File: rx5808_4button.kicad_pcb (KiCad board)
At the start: 2 copper layers, 80 x 65 mm, 60 parts, among them IC1 ATMEGA328-A, P1 CONN_01X02, P10 CONN_01X01, P11 CONN_01X01, P2 CONN_01X05, P3 CONN_02X03, P4 CONN_01X02, P5 BNC, P6 BNC, P7 CONN_01X02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

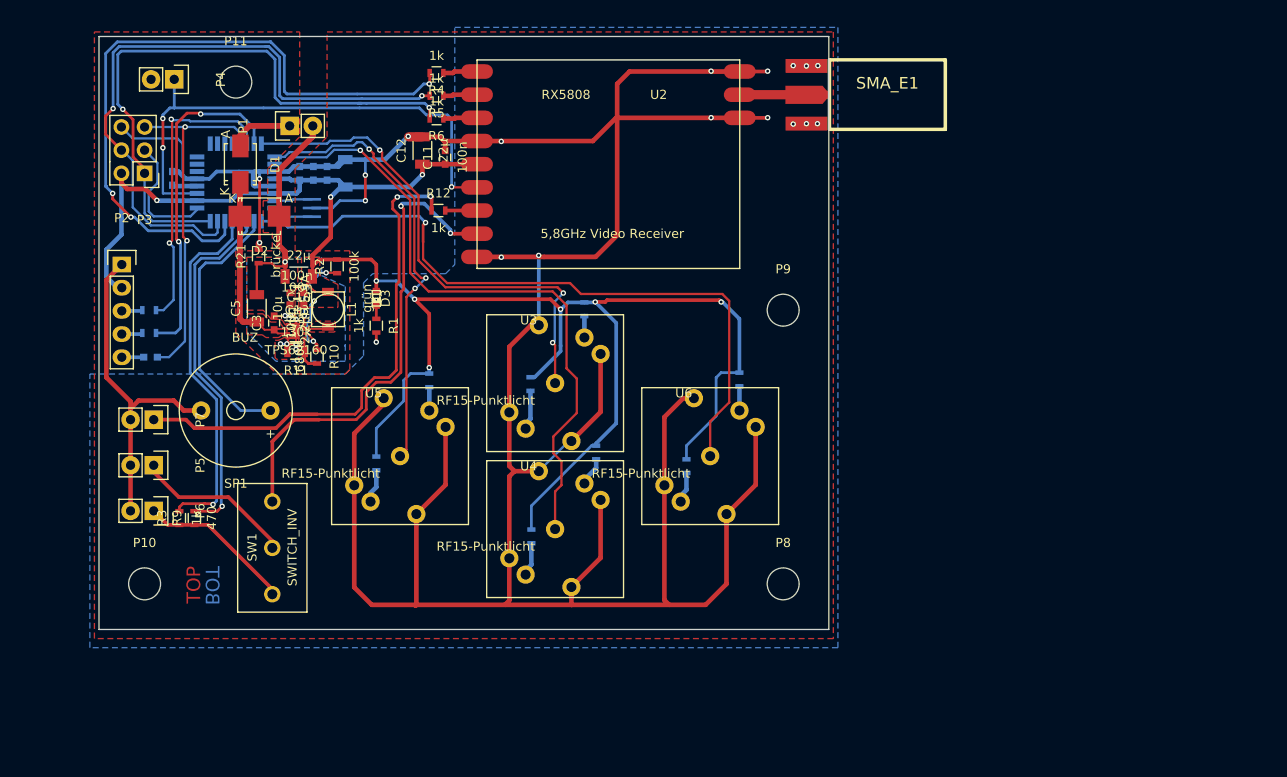
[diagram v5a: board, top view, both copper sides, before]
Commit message: symbol hinzugefügt
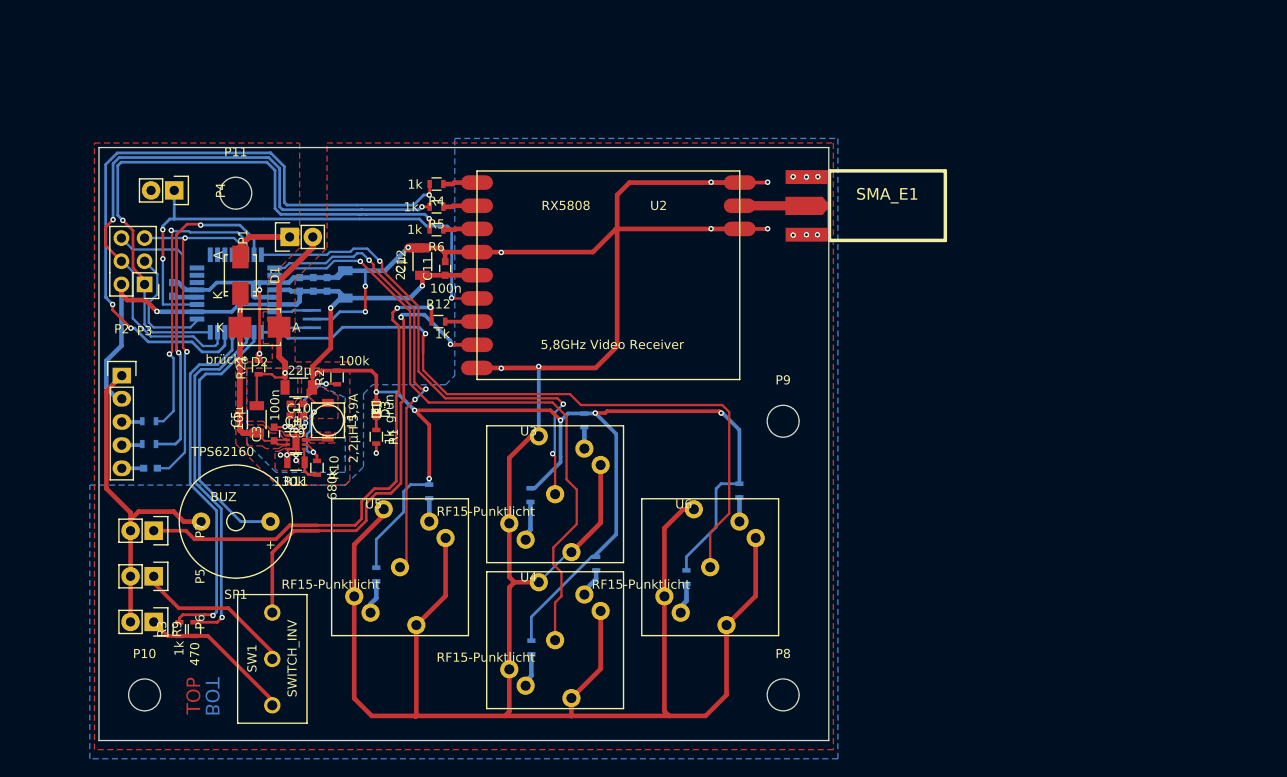
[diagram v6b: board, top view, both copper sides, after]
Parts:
- moved C13 12.2 mm to (105.7, 107.3)
- moved P10 12.2 mm to (89.0, 139.2)
- moved P6 12.2 mm to (90.0, 131.2)
- moved P8 12.2 mm to (159.0, 139.2)
- moved R10 12.2 mm to (107.9, 114.3)
- moved R14 12.2 mm to (131.3, 117.3)
- moved R15 12.2 mm to (138.5, 124.8)
- moved R19 12.2 mm to (154.2, 116.8)
- moved R20 12.2 mm to (148.4, 126.3)
- moved R21 12.2 mm to (101.5, 103.3)
- moved SW1 12.2 mm to (103.0, 135.2)
- moved U4 12.2 mm to (134.0, 133.2)
- moved Y1 12.2 mm to (107.3, 98.0)
- moved C1 12.2 mm to (92.0, 94.7)
- moved C10 12.2 mm to (105.9, 105.5)
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
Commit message: dickbutt inserted
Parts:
- added G***: LOGO, Dickbutt:Kupferdickbutt, F.Cu at (159.4, 98.4)
- P1: footprint Pin_Headers:Pin_Header_Straight_1x02 -> Sockets_MOLEX_KK-System:Socket_MOLEX-KK-RM2-54mm_Lock_2pin_straight
- moved P1 6.71 mm to (107.0, 82.6), turned to 0 degrees
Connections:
- IC1 pad 12: Net-(IC1-Pad12) -> (no net)
- IC1 pad 22: Net-(IC1-Pad22) -> (no net)
- IC1 pad 23: Net-(IC1-Pad23) -> (no net)
- IC1 pad 24: Net-(IC1-Pad24) -> (no net)
- IC1 pad 25: Net-(IC1-Pad25) -> (no net)
- IC1 pad 26: Net-(IC1-Pad26) -> (no net)
- IC1 pad 27: Net-(IC1-Pad27) -> (no net)
- IC1 pad 28: Net-(IC1-Pad28) -> (no net)
- P10 pad 1: Net-(P10-Pad1) -> (no net)
- P11 pad 1: Net-(P11-Pad1) -> (no net)
- P8 pad 1: Net-(P8-Pad1) -> (no net)
- P9 pad 1: Net-(P9-Pad1) -> (no net)
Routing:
- net GNDPWR: track 35.0 -> 41.7 mm
- net Net-(D1-Pad1): track 7.02 -> 13.1 mm
- net +12V: track 22.4 -> 24.5 mm

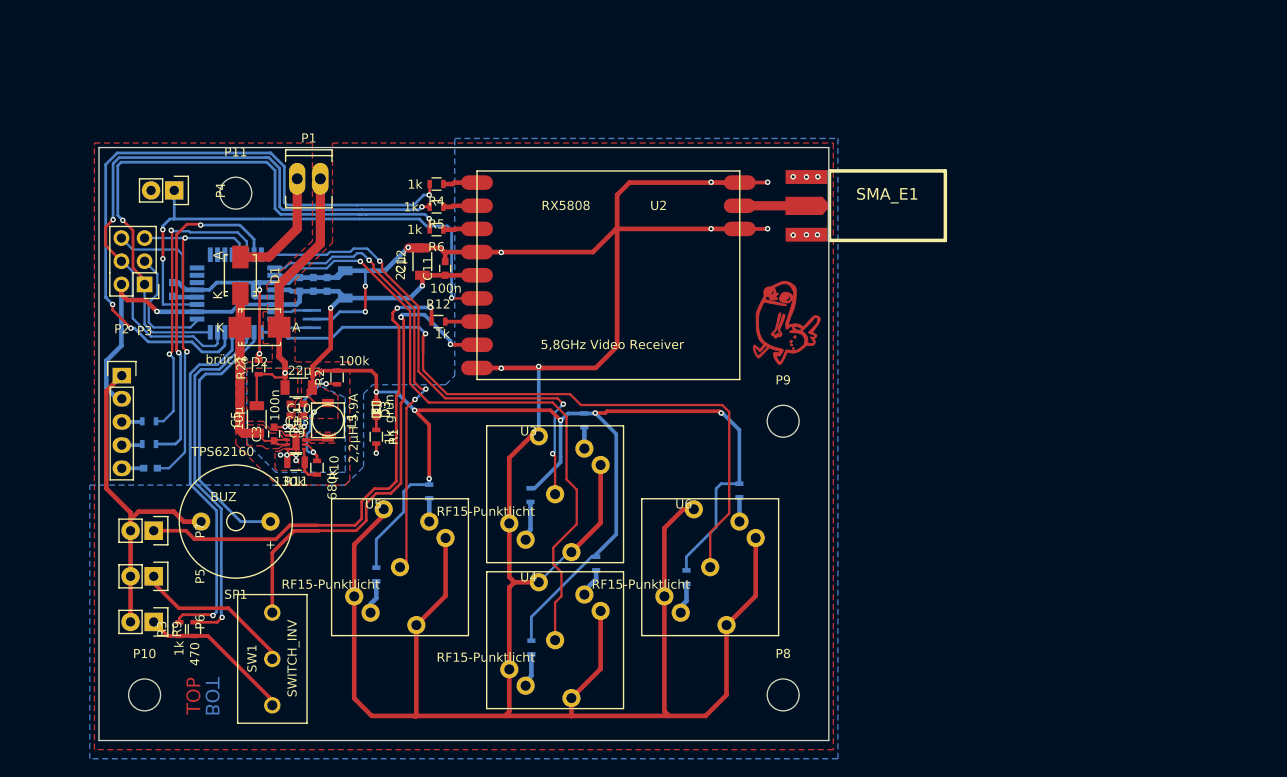
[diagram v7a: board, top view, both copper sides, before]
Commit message: Layout fertig - cinchbuchsen für Video eingebaut.
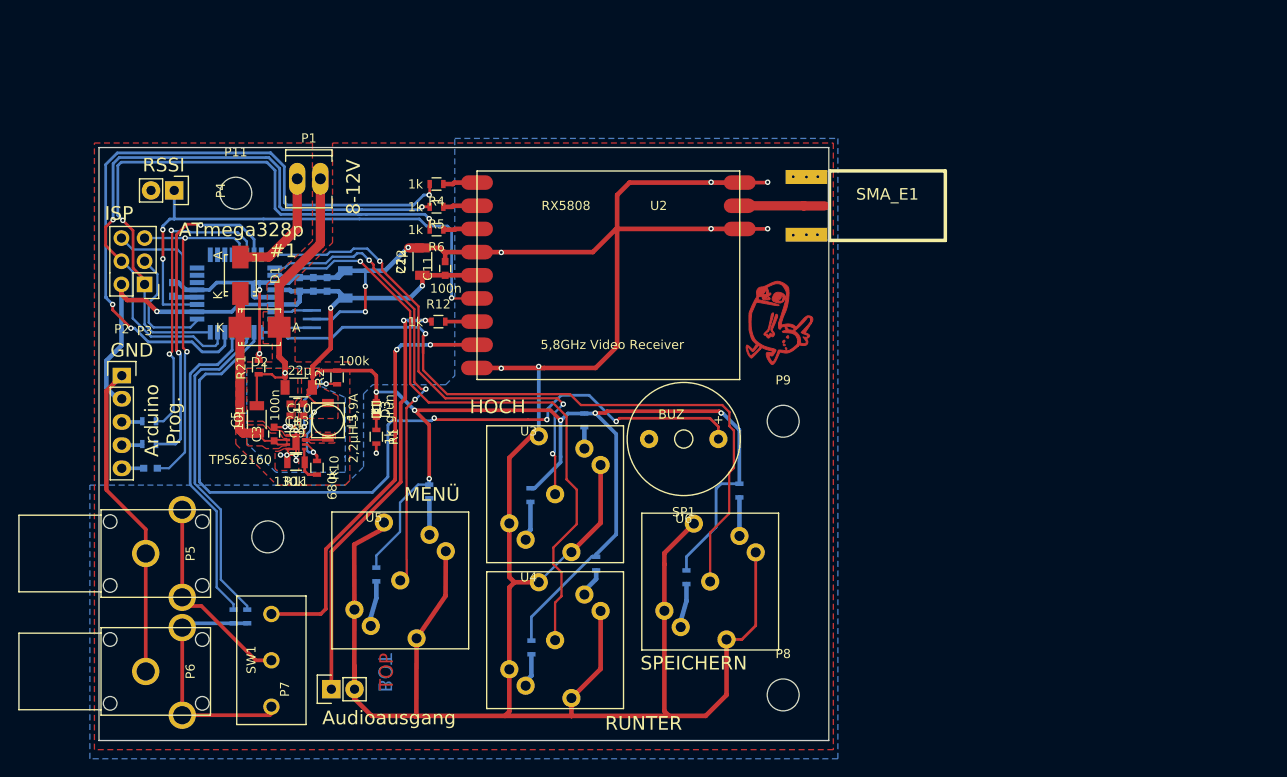
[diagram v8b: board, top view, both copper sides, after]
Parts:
- P5: footprint Pin_Headers:Pin_Header_Straight_1x02 -> Cinch_angled_mono
- P6: footprint Pin_Headers:Pin_Header_Straight_1x02 -> RCA:Cinch_angled_mono
- R3, R9: moved to B.Cu
- moved SP1 49.9 mm to (148.1, 111.1)
- moved P7 26.1 mm to (109.5, 138.6), turned to 90 degrees
- moved P10 22.0 mm to (102.5, 121.8)
- moved R3 6.10 mm to (98.8, 130.6)
- moved R9 5.95 mm to (100.2, 130.6)
- moved P6 5.50 mm to (89.1, 136.6)
- moved P5 2.65 mm to (89.1, 123.7)
- moved U6 1.58 mm to (151.0, 126.8)
- moved U5 1.45 mm to (117.0, 126.6)
- moved G*** 0.80 mm to (158.6, 98.4)
- moved SW1 0.18 mm to (102.9, 135.3)
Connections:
- IC1 pad 12: (no net) -> Net-(IC1-Pad12)
- IC1 pad 22: (no net) -> Net-(IC1-Pad22)
- IC1 pad 23: (no net) -> Net-(IC1-Pad23)
- IC1 pad 24: (no net) -> Net-(IC1-Pad24)
- IC1 pad 25: (no net) -> Net-(IC1-Pad25)
- IC1 pad 26: (no net) -> Net-(IC1-Pad26)
- IC1 pad 27: (no net) -> Net-(IC1-Pad27)
- IC1 pad 28: (no net) -> Net-(IC1-Pad28)
- P10 pad 1: (no net) -> Net-(P10-Pad1)
- P11 pad 1: (no net) -> Net-(P11-Pad1)
- P8 pad 1: (no net) -> Net-(P8-Pad1)
- P9 pad 1: (no net) -> Net-(P9-Pad1)
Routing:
- net /buzzer: track 29.4 -> 88.9 mm, vias 0 -> 3
- net /VideoOut: track 17.1 -> 27.5 mm
- net Net-(P7-Pad1): track 55.7 -> 47.0 mm
- net Net-(SW1-Pad1): track 53.6 -> 46.9 mm
- net GND: track 421.1 -> 414.5 mm
- net Net-(P5-Pad1): track 17.6 -> 22.2 mm
- net Net-(IC1-Pad13): track 39.8 -> 35.4 mm, vias 1 -> 0
- net Net-(IC1-Pad11): track 39.4 -> 36.3 mm, vias 1 -> 0
- net /save: track 76.5 -> 78.5 mm
- net Net-(R19-Pad1): track 2.65 -> 4.23 mm
- net Net-(R17-Pad1): track 2.55 -> 4.00 mm
- net /mode: track 49.1 -> 50.5 mm
- net Net-(R20-Pad1): track 3.40 -> 4.80 mm
- net Net-(R18-Pad1): track 3.70 -> 4.98 mm
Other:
- board text added: "#1"
- board text added: "8-12V"
- board text added: "ATmega328p"
- board text added: "Arduino Prog."
- board text added: "Audioausgang"
- board text added: "Design verfügbar auf Github:"
- board text added: "GND"
- board text added: "HOCH"
- board text added: "ISP"
- board text added: "MENÜ"
- board text added: "RSSI"
- board text added: "RUNTER"
- board text added: "SPEICHERN"
- board text added: "https://github.com/Virtex7/RX5808"
